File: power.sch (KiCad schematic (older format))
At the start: 15 parts

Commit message: sch has been finished
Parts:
- removed P?: CONN_01X02, symbol CONN_01X02
- added P2: CONN_1x2, symbol CONN_1x2
- P1: renamed from P?; symbol CONN_01X02 -> CONN_01X02-RESCUE-BBBCanFly
- R1, R2: renamed from R?; value R -> 10k
- gave numbers to parts that had none: 11
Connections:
- net labels removed: +24V, +5V
- wire segments 35 -> 34
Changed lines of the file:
@@
 EESchema Schematic File Version 2
+LIBS:BBBCanFly-rescue
 LIBS:power
 LIBS:device
@@
 $EndDescr
 $Comp
-L CONN_01X02 P?
+L CONN_01X02-RESCUE-BBBCanFly P1
 U 1 1 570FB603
 P 750 950
-F 0 "P?" H 750 1100 50  0000 C CNN
+AR Path="/570FB603" Ref="P1"  Part="1"
+AR Path="/570FB5F5/570FB603" Ref="P1"  Part="1"
+F 0 "P1" H 750 1100 50  0000 C CNN
 F 1 "CONN_01X02" V 850 950 50  0001 C CNN
 F 2 "" H 750 950 50  0000 C CNN
@@
 $EndComp
 $Comp
-L +24V #PWR?
-U 1 1 570FD143
-P 1000 850
-F 0 "#PWR?" H 1000 700 50  0001 C CNN
-F 1 "+24V" H 1000 990 50  0000 C CNN
-F 2 "" H 1000 850 50  0000 C CNN
-F 3 "" H 1000 850 50  0000 C CNN
-	1    1000 850
-	1    0    0    -1
-$EndComp
-$Comp
-L HT7465 U?
+L HT7465 U1
 U 1 1 5718CFDE
 P 1900 1600
-F 0 "U?" H 1950 1650 60  0000 C CNN
+F 0 "U1" H 1950 1650 60  0000 C CNN
 F 1 "HT7465" H 2300 1250 60  0000 C CNN
 F 2 "" H 1900 1600 60  0000 C CNN
@@
 $EndComp
 $Comp
-L C C?
+L C C1
 U 1 1 5718D07D
 P 1250 1150
-F 0 "C?" H 1275 1250 50  0000 L CNN
+F 0 "C1" H 1275 1250 50  0000 L CNN
 F 1 "10u" H 1275 1050 50  0000 L CNN
 F 2 "" H 1288 1000 50  0000 C CNN
@@
 $EndComp
 $Comp
-L GND #PWR?
+L GND #PWR1
 U 1 1 5718D30A
 P 1000 1450
-F 0 "#PWR?" H 1000 1200 50  0001 C CNN
+F 0 "#PWR1" H 1000 1200 50  0001 C CNN
 F 1 "GND" H 1000 1300 50  0000 C CNN
 F 2 "" H 1000 1450 50  0000 C CNN
@@
 $EndComp
 $Comp
-L C C?
+L C C3
 U 1 1 5720B90E
 P 2650 1100
-F 0 "C?" H 2675 1200 50  0000 L CNN
+F 0 "C3" H 2675 1200 50  0000 L CNN
 F 1 "10n" H 2675 1000 50  0000 L CNN
 F 2 "" H 2688 950 50  0000 C CNN
@@
 $EndComp
 $Comp
-L R R?
+L R R1
 U 1 1 5720BEF4
 P 1600 1550
-F 0 "R?" V 1680 1550 50  0000 C CNN
-F 1 "R" V 1600 1550 50  0000 C CNN
+F 0 "R1" V 1680 1550 50  0000 C CNN
+F 1 "10k" V 1600 1550 50  0000 C CNN
 F 2 "" V 1530 1550 50  0000 C CNN
 F 3 "" H 1600 1550 50  0000 C CNN
@@
 $EndComp
 $Comp
-L R R?
+L R R2
 U 1 1 5720BF43
 P 1600 2150
-F 0 "R?" V 1680 2150 50  0000 C CNN
-F 1 "R" V 1600 2150 50  0000 C CNN
+F 0 "R2" V 1680 2150 50  0000 C CNN
+F 1 "10k" V 1600 2150 50  0000 C CNN
 F 2 "" V 1530 2150 50  0000 C CNN
 F 3 "" H 1600 2150 50  0000 C CNN
@@
 $EndComp
 $Comp
-L GND #PWR?
+L GND #PWR2
 U 1 1 5720BFBE
 P 2450 3550
-F 0 "#PWR?" H 2450 3300 50  0001 C CNN
+F 0 "#PWR2" H 2450 3300 50  0001 C CNN
 F 1 "GND" H 2450 3400 50  0000 C CNN
 F 2 "" H 2450 3550 50  0000 C CNN
@@
 $EndComp
 $Comp
-L INDUCTOR L?
+L INDUCTOR L1
 U 1 1 5720C81B
 P 3350 1850
-F 0 "L?" V 3300 1850 50  0000 C CNN
+F 0 "L1" V 3300 1850 50  0000 C CNN
 F 1 "15uH" V 3450 1850 50  0000 C CNN
 F 2 "" H 3350 1850 50  0000 C CNN
@@
 $EndComp
 $Comp
-L +5V #PWR?
-U 1 1 5720C90B
-P 3850 1750
-F 0 "#PWR?" H 3850 1600 50  0001 C CNN
-F 1 "+5V" H 3850 1890 50  0000 C CNN
-F 2 "" H 3850 1750 50  0000 C CNN
-F 3 "" H 3850 1750 50  0000 C CNN
-	1    3850 1750
-	1    0    0    -1
-$EndComp
-$Comp
-L R R?
+L R R5
 U 1 1 5720C9C3
 P 3500 2050
-F 0 "R?" V 3580 2050 50  0000 C CNN
+F 0 "R5" V 3580 2050 50  0000 C CNN
 F 1 "44.2k" V 3500 2050 50  0000 C CNN
 F 2 "" V 3430 2050 50  0000 C CNN
@@
 $EndComp
 $Comp
-L R R?
+L R R4
 U 1 1 5720CA16
 P 3300 2800
-F 0 "R?" V 3380 2800 50  0000 C CNN
+F 0 "R4" V 3380 2800 50  0000 C CNN
 F 1 "10k" V 3300 2800 50  0000 C CNN
 F 2 "" V 3230 2800 50  0000 C CNN
@@
 $EndComp
 $Comp
-L D D?
+L D D1
 U 1 1 5720CC1C
 P 3050 2800
-F 0 "D?" H 3050 2900 50  0000 C CNN
+F 0 "D1" H 3050 2900 50  0000 C CNN
 F 1 "B230A" H 3050 2700 50  0000 C CNN
 F 2 "" H 3050 2800 50  0000 C CNN
@@
 $EndComp
 $Comp
-L R R?
+L R R3
 U 1 1 5720CFB5
 P 2450 2800
-F 0 "R?" V 2530 2800 50  0000 C CNN
+F 0 "R3" V 2530 2800 50  0000 C CNN
 F 1 "18k" V 2450 2800 50  0000 C CNN
 F 2 "" V 2380 2800 50  0000 C CNN
@@
 $EndComp
 $Comp
-L C C?
+L C C2
 U 1 1 5720CFF7
 P 2450 3250
-F 0 "C?" H 2475 3350 50  0000 L CNN
+F 0 "C2" H 2475 3350 50  0000 L CNN
 F 1 "1.5n" H 2475 3150 50  0000 L CNN
 F 2 "" H 2488 3100 50  0000 C CNN
@@
 $EndComp
 $Comp
-L C C?
+L C C4
 U 1 1 5720D4EF
 P 2750 3000
-F 0 "C?" H 2775 3100 50  0000 L CNN
+F 0 "C4" H 2775 3100 50  0000 L CNN
 F 1 "1n" H 2775 2900 50  0000 L CNN
 F 2 "" H 2788 2850 50  0000 C CNN
@@
 $EndComp
 $Comp
-L C C?
+L C C5
 U 1 1 5720D563
 P 3850 2800
-F 0 "C?" H 3875 2900 50  0000 L CNN
+F 0 "C5" H 3875 2900 50  0000 L CNN
 F 1 "22u" H 3875 2700 50  0000 L CNN
 F 2 "" H 3888 2650 50  0000 C CNN
@@
 	1    0    0    -1
 $EndComp
-Wire Wire Line
-	1000 900  1000 850
+$Comp
+L GND #PWR3
+U 1 1 57651402
+P 4050 2050
+F 0 "#PWR3" H 4050 1800 50  0001 C CNN
+F 1 "GND" H 4050 1900 50  0000 C CNN
+F 2 "" H 4050 2050 50  0000 C CNN
+F 3 "" H 4050 2050 50  0000 C CNN
+	1    4050 2050
+	1    0    0    -1
+$EndComp
+Text HLabel 1600 900  0    60   Output ~ 0
+24V
 Wire Wire Line
 	950  1000 1000 1000
 Wire Wire Line
 	1000 1000 1000 1450
-Connection ~ 1000 900
 Connection ~ 1250 900
 Wire Wire Line
@@
 Wire Wire Line
 	3650 2050 3850 2050
-Wire Wire Line
-	3850 1750 3850 2650
 Connection ~ 3850 2050
 Wire Wire Line
@@
 Wire Wire Line
 	1250 1400 1250 1300
-$Comp
-L CONN_01X02 P?
-U 1 1 5765136B
-P 4300 1900
-F 0 "P?" H 4300 2050 50  0000 C CNN
-F 1 "CONN_01X02" V 4400 1900 50  0000 C CNN
-F 2 "" H 4300 1900 50  0000 C CNN
-F 3 "" H 4300 1900 50  0000 C CNN
-	1    4300 1900
-	1    0    0    -1
-$EndComp
-$Comp
-L GND #PWR?
-U 1 1 57651402
-P 4050 2150
-F 0 "#PWR?" H 4050 1900 50  0001 C CNN
-F 1 "GND" H 4050 2000 50  0000 C CNN
-F 2 "" H 4050 2150 50  0000 C CNN
-F 3 "" H 4050 2150 50  0000 C CNN
-	1    4050 2150
-	1    0    0    -1
-$EndComp
 Wire Wire Line
 	4100 1950 4050 1950
 Wire Wire Line
-	4050 1950 4050 2150
-Text GLabel 1600 900  1    60   Output ~ 0
-24V
+	4050 1950 4050 2050
+Wire Wire Line
+	3850 2650 3850 1850
+$Comp
+L CONN_1x2 P2
+U 1 1 57B25287
+P 4350 1750
+F 0 "P2" H 4350 1750 60  0000 C CNN
+F 1 "CONN_1x2" V 4450 1600 60  0000 C CNN
+F 2 "" H 4350 1750 60  0000 C CNN
+F 3 "" H 4350 1750 60  0000 C CNN
+	1    4350 1750
+	1    0    0    -1
+$EndComp
 $EndSCHEMATC

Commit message: pcb finished.
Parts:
- C1: footprint (none) -> Capacitors_SMD:C_1812
- C2, C3, C4, C5: footprint (none) -> Capacitors_SMD:C_0805
- D1: footprint (none) -> Diodes_SMD:DO-214BA
- L1: footprint (none) -> Capacitors_SMD:C_1206
- P1, P2: footprint (none) -> Pin_Headers:Pin_Header_Straight_1x02
- R1, R2, R3, R4, R5: footprint (none) -> Resistors_SMD:R_0805
- U1: footprint (none) -> Power_Integrations:SO-8
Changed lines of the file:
@@
 U 1 1 570FB603
 P 750 950
-AR Path="/570FB603" Ref="P1"  Part="1"
-AR Path="/570FB5F5/570FB603" Ref="P1"  Part="1"
 F 0 "P1" H 750 1100 50  0000 C CNN
 F 1 "CONN_01X02" V 850 950 50  0001 C CNN
-F 2 "" H 750 950 50  0000 C CNN
+F 2 "Pin_Headers:Pin_Header_Straight_1x02" H 750 950 50  0001 C CNN
 F 3 "" H 750 950 50  0000 C CNN
 	1    750  950
@@
 F 0 "U1" H 1950 1650 60  0000 C CNN
 F 1 "HT7465" H 2300 1250 60  0000 C CNN
-F 2 "" H 1900 1600 60  0000 C CNN
+F 2 "Power_Integrations:SO-8" H 1900 1600 60  0001 C CNN
 F 3 "" H 1900 1600 60  0000 C CNN
 	1    1900 1600
@@
 F 0 "C1" H 1275 1250 50  0000 L CNN
 F 1 "10u" H 1275 1050 50  0000 L CNN
-F 2 "" H 1288 1000 50  0000 C CNN
+F 2 "Capacitors_SMD:C_1812" H 1288 1000 50  0001 C CNN
 F 3 "" H 1250 1150 50  0000 C CNN
 	1    1250 1150
@@
 $EndComp
 $Comp
-L GND #PWR1
+L GND #PWR01
 U 1 1 5718D30A
 P 1000 1450
-F 0 "#PWR1" H 1000 1200 50  0001 C CNN
+F 0 "#PWR01" H 1000 1200 50  0001 C CNN
 F 1 "GND" H 1000 1300 50  0000 C CNN
 F 2 "" H 1000 1450 50  0000 C CNN
@@
 F 0 "C3" H 2675 1200 50  0000 L CNN
 F 1 "10n" H 2675 1000 50  0000 L CNN
-F 2 "" H 2688 950 50  0000 C CNN
+F 2 "Capacitors_SMD:C_0805" H 2688 950 50  0001 C CNN
 F 3 "" H 2650 1100 50  0000 C CNN
 	1    2650 1100
@@
 F 0 "R1" V 1680 1550 50  0000 C CNN
 F 1 "10k" V 1600 1550 50  0000 C CNN
-F 2 "" V 1530 1550 50  0000 C CNN
+F 2 "Resistors_SMD:R_0805" V 1530 1550 50  0001 C CNN
 F 3 "" H 1600 1550 50  0000 C CNN
 	1    1600 1550
@@
 F 0 "R2" V 1680 2150 50  0000 C CNN
 F 1 "10k" V 1600 2150 50  0000 C CNN
-F 2 "" V 1530 2150 50  0000 C CNN
+F 2 "Resistors_SMD:R_0805" V 1530 2150 50  0001 C CNN
 F 3 "" H 1600 2150 50  0000 C CNN
 	1    1600 2150
@@
 $EndComp
 $Comp
-L GND #PWR2
+L GND #PWR02
 U 1 1 5720BFBE
 P 2450 3550
-F 0 "#PWR2" H 2450 3300 50  0001 C CNN
+F 0 "#PWR02" H 2450 3300 50  0001 C CNN
 F 1 "GND" H 2450 3400 50  0000 C CNN
 F 2 "" H 2450 3550 50  0000 C CNN
@@
 F 0 "L1" V 3300 1850 50  0000 C CNN
 F 1 "15uH" V 3450 1850 50  0000 C CNN
-F 2 "" H 3350 1850 50  0000 C CNN
+F 2 "Capacitors_SMD:C_1206" H 3350 1850 50  0001 C CNN
 F 3 "" H 3350 1850 50  0000 C CNN
 	1    3350 1850
@@
 F 0 "R5" V 3580 2050 50  0000 C CNN
 F 1 "44.2k" V 3500 2050 50  0000 C CNN
-F 2 "" V 3430 2050 50  0000 C CNN
+F 2 "Resistors_SMD:R_0805" V 3430 2050 50  0001 C CNN
 F 3 "" H 3500 2050 50  0000 C CNN
 	1    3500 2050
@@
 F 0 "R4" V 3380 2800 50  0000 C CNN
 F 1 "10k" V 3300 2800 50  0000 C CNN
-F 2 "" V 3230 2800 50  0000 C CNN
+F 2 "Resistors_SMD:R_0805" V 3230 2800 50  0001 C CNN
 F 3 "" H 3300 2800 50  0000 C CNN
 	1    3300 2800
@@
 F 0 "D1" H 3050 2900 50  0000 C CNN
 F 1 "B230A" H 3050 2700 50  0000 C CNN
-F 2 "" H 3050 2800 50  0000 C CNN
+F 2 "Diodes_SMD:DO-214BA" H 3050 2800 50  0001 C CNN
 F 3 "" H 3050 2800 50  0000 C CNN
 	1    3050 2800
@@
 F 0 "R3" V 2530 2800 50  0000 C CNN
 F 1 "18k" V 2450 2800 50  0000 C CNN
-F 2 "" V 2380 2800 50  0000 C CNN
+F 2 "Resistors_SMD:R_0805" V 2380 2800 50  0001 C CNN
 F 3 "" H 2450 2800 50  0000 C CNN
 	1    2450 2800
@@
 F 0 "C2" H 2475 3350 50  0000 L CNN
 F 1 "1.5n" H 2475 3150 50  0000 L CNN
-F 2 "" H 2488 3100 50  0000 C CNN
+F 2 "Capacitors_SMD:C_0805" H 2488 3100 50  0001 C CNN
 F 3 "" H 2450 3250 50  0000 C CNN
 	1    2450 3250
@@
 F 0 "C4" H 2775 3100 50  0000 L CNN
 F 1 "1n" H 2775 2900 50  0000 L CNN
-F 2 "" H 2788 2850 50  0000 C CNN
+F 2 "Capacitors_SMD:C_0805" H 2788 2850 50  0001 C CNN
 F 3 "" H 2750 3000 50  0000 C CNN
 	1    2750 3000
@@
 F 0 "C5" H 3875 2900 50  0000 L CNN
 F 1 "22u" H 3875 2700 50  0000 L CNN
-F 2 "" H 3888 2650 50  0000 C CNN
+F 2 "Capacitors_SMD:C_0805" H 3888 2650 50  0001 C CNN
 F 3 "" H 3850 2800 50  0000 C CNN
 	1    3850 2800
@@
 $EndComp
 $Comp
-L GND #PWR3
+L GND #PWR03
 U 1 1 57651402
 P 4050 2050
-F 0 "#PWR3" H 4050 1800 50  0001 C CNN
+F 0 "#PWR03" H 4050 1800 50  0001 C CNN
 F 1 "GND" H 4050 1900 50  0000 C CNN
 F 2 "" H 4050 2050 50  0000 C CNN
@@
 F 0 "P2" H 4350 1750 60  0000 C CNN
 F 1 "CONN_1x2" V 4450 1600 60  0000 C CNN
-F 2 "" H 4350 1750 60  0000 C CNN
+F 2 "Pin_Headers:Pin_Header_Straight_1x02" H 4350 1750 60  0001 C CNN
 F 3 "" H 4350 1750 60  0000 C CNN
 	1    4350 1750

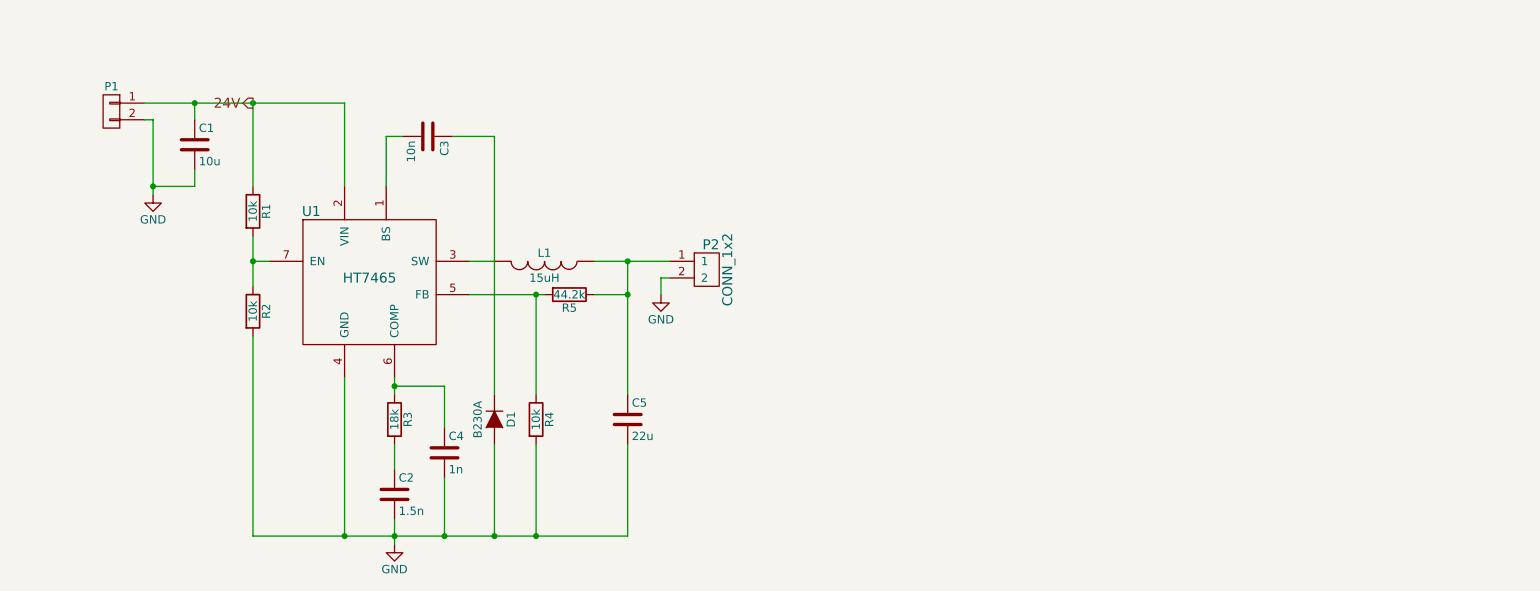
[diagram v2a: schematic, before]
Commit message: modified power supply program
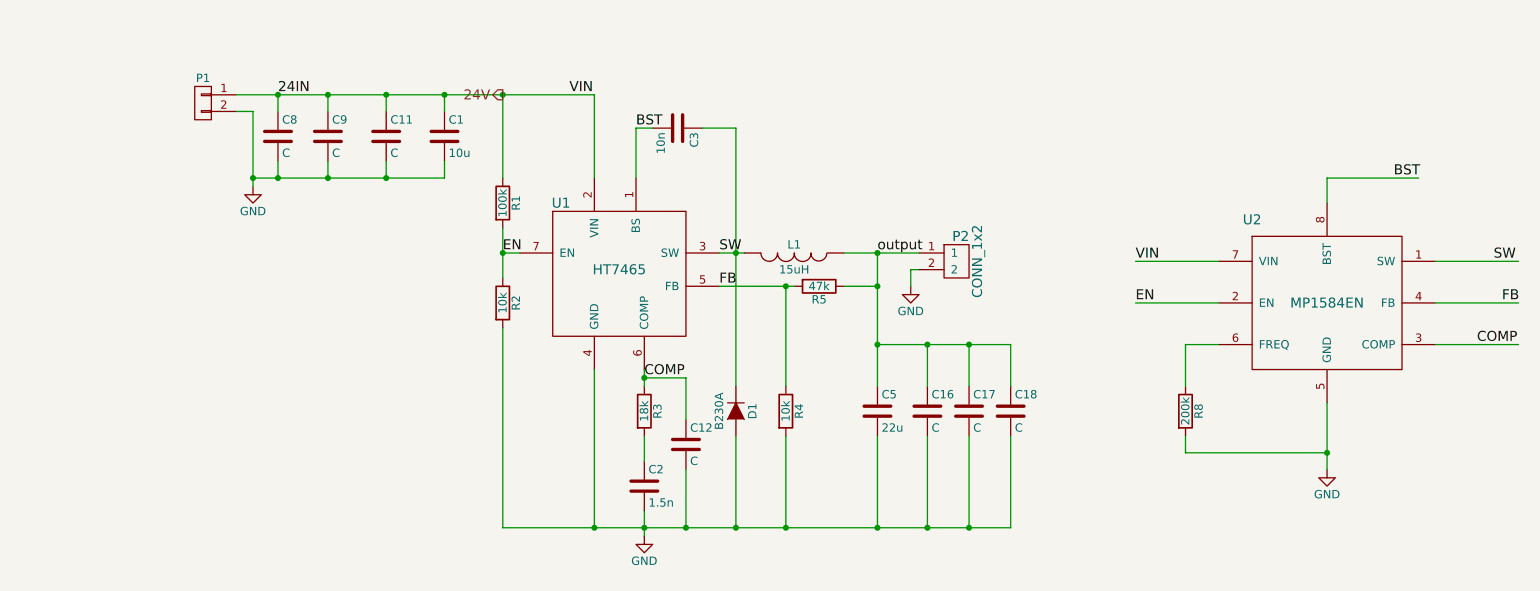
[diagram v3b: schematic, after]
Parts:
- removed C4: 1n, Capacitors_SMD:C_0805, symbol C
- added C11, C16: C, Capacitors_SMD:C_1812_HandSoldering, symbol C
- added C12, C17, C18, C8, C9: C, Capacitors_SMD:C_0805_HandSoldering, symbol C
- added R8: 200k, Resistors_SMD:R_0805_HandSoldering, symbol R
- added U2: MP1584EN, Housings_SOIC:SOIC-8-1EP_3.9x4.9mm_Pitch1.27mm, symbol MP1584EN
- C1: footprint Capacitors_SMD:C_1812 -> Capacitors_SMD:c_elec_5x5.7
- C2, C3: footprint Capacitors_SMD:C_0805 -> Capacitors_SMD:C_0805_HandSoldering
- C5: footprint Capacitors_SMD:C_0805 -> Capacitors_SMD:c_elec_5x5.7
- D1: footprint Diodes_SMD:DO-214BA -> Diodes_SMD:DO-214AB
- L1: footprint Capacitors_SMD:C_1206 -> Inductors_NEOSID:Neosid_Inductor_SM-NE127
- R1: value 10k -> 100k; footprint Resistors_SMD:R_0805 -> Resistors_SMD:R_0805_HandSoldering
- R2, R3, R4: footprint Resistors_SMD:R_0805 -> Resistors_SMD:R_0805_HandSoldering
- R5: value 44.2k -> 47k; footprint Resistors_SMD:R_0805 -> Resistors_SMD:R_0805_HandSoldering
- U1: footprint Power_Integrations:SO-8 -> Housings_SOIC:SOIC-8-1EP_3.9x4.9mm_Pitch1.27mm
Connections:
- net labels added: 24IN, BST, COMP, EN, FB, SW, VIN, output
- wire segments 34 -> 59
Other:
- moved on the sheet: C1, C2, C3, C5, D1, L1, P1, P2, R1, R2, R3, R4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

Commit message: latest version
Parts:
- C5: footprint Capacitors_SMD:c_elec_5x5.7 -> Capacitors_SMD:c_elec_4x5.3
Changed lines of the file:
@@
 F 0 "C5" H 5375 2850 50  0000 L CNN
 F 1 "22u" H 5375 2650 50  0000 L CNN
-F 2 "Capacitors_SMD:c_elec_5x5.7" H 5388 2600 50  0001 C CNN
+F 2 "Capacitors_SMD:c_elec_4x5.3" H 5388 2600 50  0001 C CNN
 F 3 "" H 5350 2750 50  0000 C CNN
 	1    5350 2750
